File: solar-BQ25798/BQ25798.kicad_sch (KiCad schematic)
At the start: 34 parts, among them U1701 BQ25798RQMR

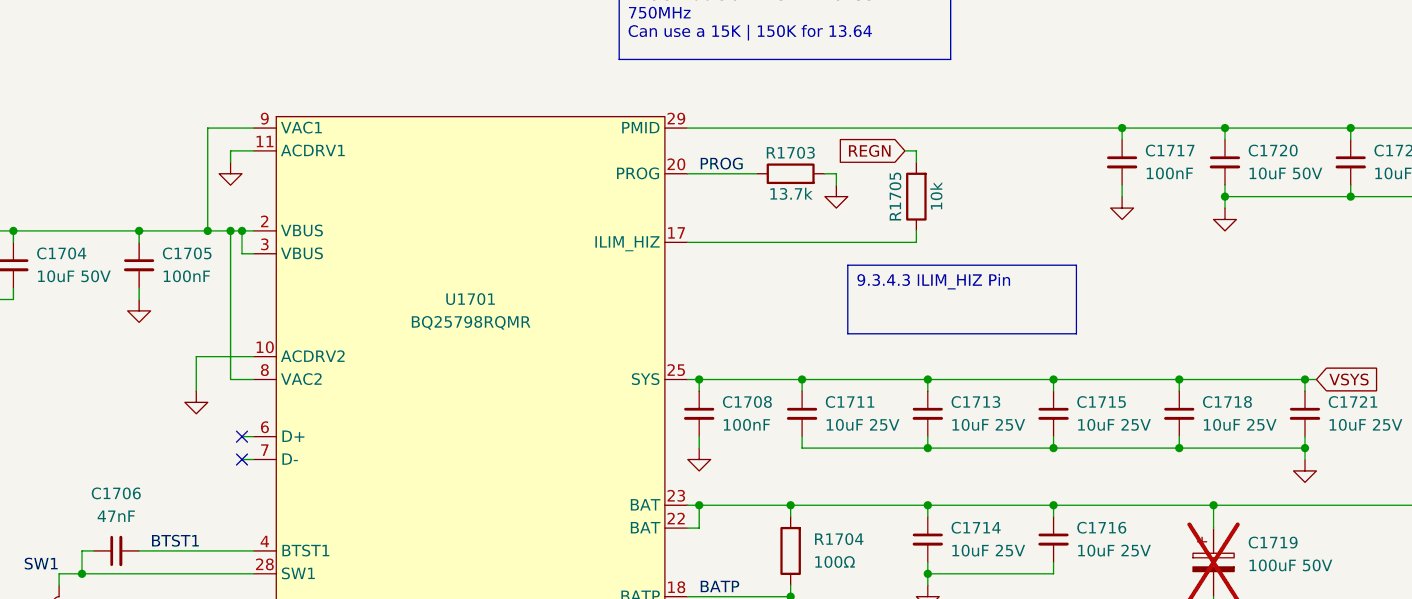
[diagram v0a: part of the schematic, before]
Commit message: Reduce number of different resistor and capacitor values
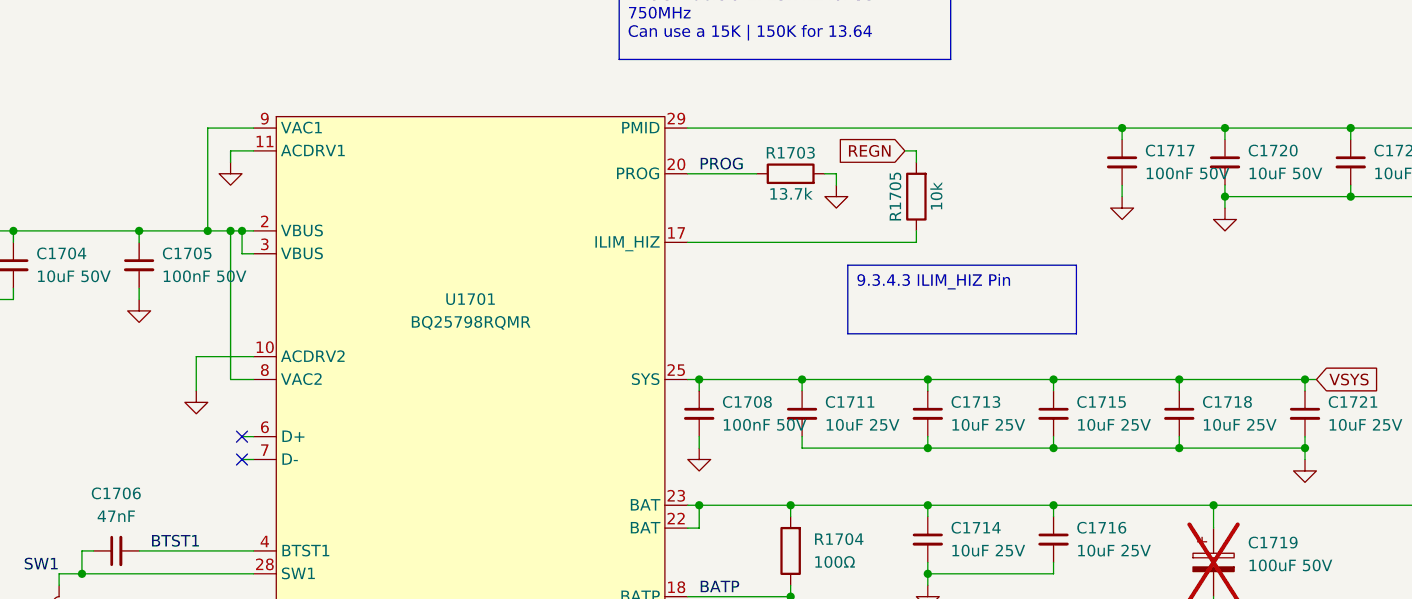
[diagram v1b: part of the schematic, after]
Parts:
- C1705, C1708, C1717: value 100nF -> 100nF 50V
- C1709: footprint Capacitor_SMD:C_0603_1608Metric -> Capacitor_SMD:C_0402_1005Metric; LCSC Part C19666 -> C23733
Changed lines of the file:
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@@
 			)
 		)
-		(property "Value" "100nF"
+		(property "Value" "100nF 50V"
 			(at 233.68 43.1862 0)
 			(show_name no)
@@
 			)
 		)
-		(property "Value" "100nF"
+		(property "Value" "100nF 50V"
 			(at 124.46 54.6162 0)
 			(show_name no)
@@
 			)
 		)
-		(property "Value" "100nF"
+		(property "Value" "100nF 50V"
 			(at 186.69 71.1262 0)
 			(show_name no)
@@
 			)
 		)
-		(property "Footprint" "Capacitor_SMD:C_0603_1608Metric"
+		(property "Footprint" "Capacitor_SMD:C_0402_1005Metric"
 			(at 187.96 127 0)
 			(hide yes)
@@
 			)
 		)
-		(property "LCSC Part" "C19666"
+		(property "LCSC Part" "C23733"
 			(at 187.96 127 0)
 			(hide yes)

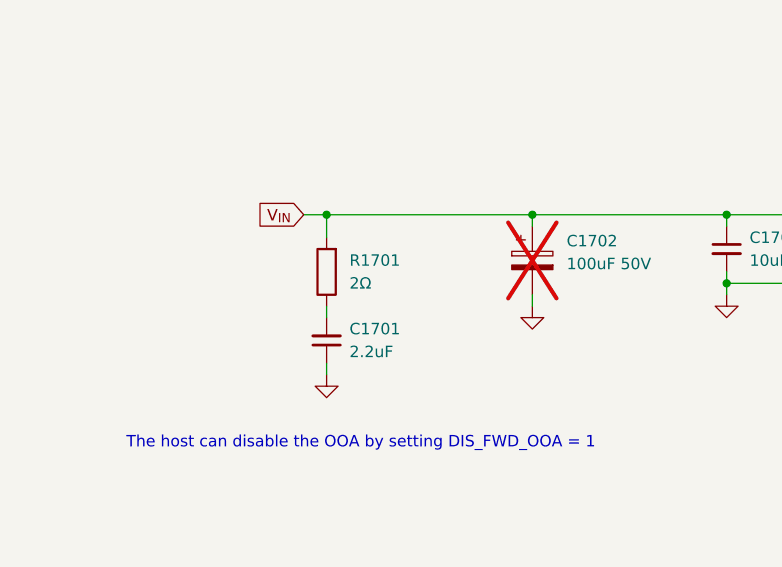
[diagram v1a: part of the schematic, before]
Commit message: Update components LCSC parts
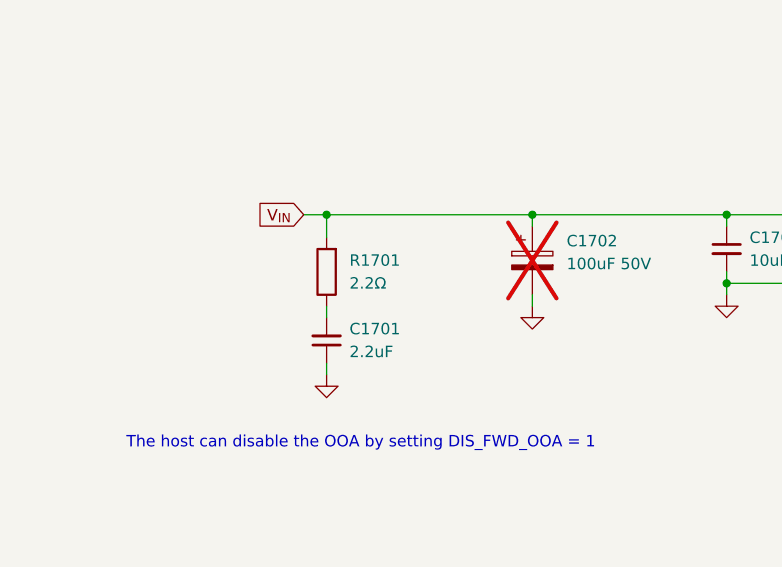
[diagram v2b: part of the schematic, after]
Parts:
- R1701: value 2Ω -> 2.2Ω; LCSC Part C17606 -> C17521
- R1707: LCSC Part C477765 -> C5948099
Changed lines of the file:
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@@
 			)
 		)
-		(property "Value" "2Ω"
+		(property "Value" "2.2Ω"
 			(at 52.07 57.1499 0)
 			(show_name no)
@@
 			)
 		)
-		(property "LCSC Part" "C17606"
+		(property "LCSC Part" "C17521"
 			(at 49.53 55.88 0)
 			(hide yes)
@@
 			)
 		)
-		(property "LCSC Part" "C477765"
+		(property "LCSC Part" "C5948099"
 			(at 217.17 109.22 0)
 			(hide yes)

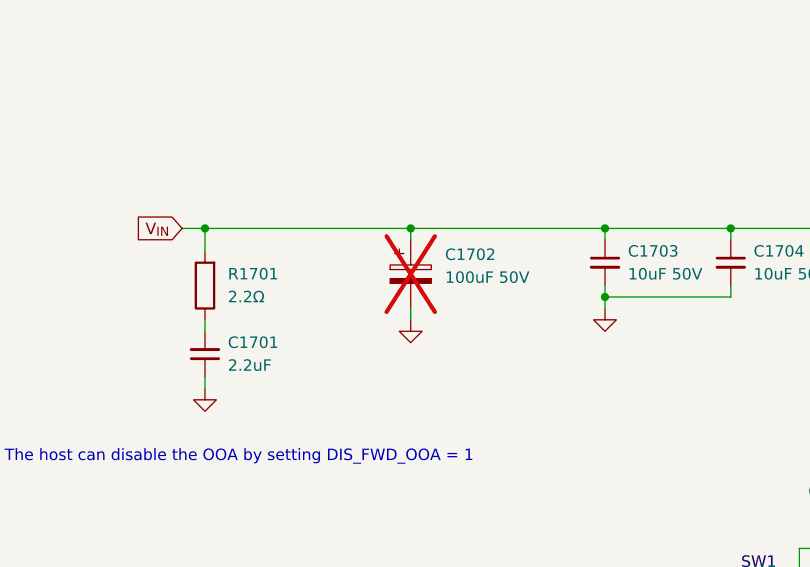
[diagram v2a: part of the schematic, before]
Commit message: Add heating element
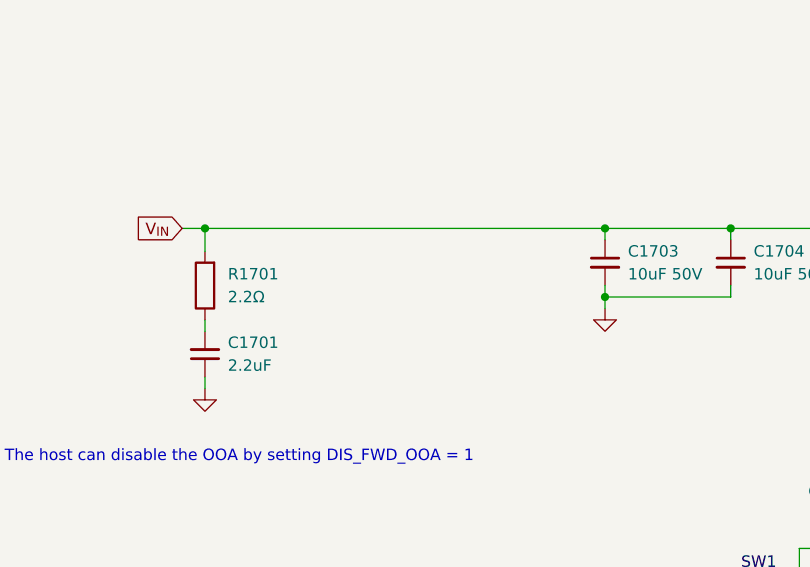
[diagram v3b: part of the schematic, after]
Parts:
- removed C1702: 100uF 50V, Capacitor_THT:CP_Radial_D6.3mm_P2.50mm, symbol Device:C_Polarized
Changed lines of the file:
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@@
 	)
 	(junction
-		(at 72.39 49.53)
-		(diameter 0)
-		(color 0 0 0 0)
-	)
-	(junction
 		(at 209.55 87.63)
 		(diameter 0)
@@
 	(wire
 		(pts
-			(xy 49.53 49.53) (xy 72.39 49.53)
-		)
-		(stroke
-			(width 0)
-			(type default)
-		)
-	)
-	(wire
-		(pts
-			(xy 72.39 49.53) (xy 72.39 50.8)
+			(xy 49.53 49.53) (xy 93.98 49.53)
 		)
 		(stroke
@@
 	(wire
 		(pts
-			(xy 72.39 49.53) (xy 93.98 49.53)
-		)
-		(stroke
-			(width 0)
-			(type default)
-		)
-	)
-	(wire
-		(pts
 			(xy 133.35 74.93) (xy 134.62 74.93)
 		)
@@
 	(wire
 		(pts
-			(xy 72.39 58.42) (xy 72.39 59.69)
-		)
-		(stroke
-			(width 0)
-			(type default)
-		)
-	)
-	(wire
-		(pts
 			(xy 132.08 66.04) (xy 134.62 66.04)
 		)
@@
 	)
 	(symbol
-		(lib_id "Device:C_Polarized")
-		(at 72.39 54.61 0)
-		(unit 1)
-		(body_style 1)
-		(exclude_from_sim no)
-		(in_bom no)
-		(on_board yes)
-		(in_pos_files yes)
-		(dnp yes)
-		(fields_autoplaced yes)
-		(property "Reference" "C1702"
-			(at 76.2 52.4509 0)
-			(show_name no)
-			(do_not_autoplace no)
-			(effects
-				(font
-					(size 1.27 1.27)
-				)
-				(justify left)
-			)
-		)
-		(property "Value" "100uF 50V"
-			(at 76.2 54.9909 0)
-			(show_name no)
-			(do_not_autoplace no)
-			(effects
-				(font
-					(size 1.27 1.27)
-				)
-				(justify left)
-			)
-		)
-		(property "Footprint" "Capacitor_THT:CP_Radial_D6.3mm_P2.50mm"
-			(at 73.3552 58.42 0)
-			(hide yes)
-			(show_name no)
-			(do_not_autoplace no)
-			(effects
-				(font
-					(size 1.27 1.27)
-				)
-			)
-		)
-		(property "Datasheet" ""
-			(at 72.39 54.61 0)
-			(hide yes)
-			(show_name no)
-			(do_not_autoplace no)
-			(effects
-				(font
-					(size 1.27 1.27)
-				)
-			)
-		)
-		(property "Description" "Polarized capacitor"
-			(at 72.39 54.61 0)
-			(hide yes)
-			(show_name no)
-			(do_not_autoplace no)
-			(effects
-				(font
-					(size 1.27 1.27)
-				)
-			)
-		)
-		(pin "2"
-		)
-		(pin "1"
-		)
-		(instances
-			(project "solar-BQ25798"
-				(path "/822b745e-d66e-4222-a6d2-360780548724/d84bfbfe-22f6-48d9-a29f-b45e9820ae80"
-					(reference "C1702")
-					(unit 1)
-				)
-			)
-		)
-	)
-	(symbol
 		(lib_id "Device:C_Small")
 		(at 198.12 105.41 270)
@@
 					(unit 1)
 				)
-			)
-		)
-	)
-	(symbol
-		(lib_id "power:GND")
-		(at 72.39 59.69 0)
-		(unit 1)
-		(body_style 1)
-		(exclude_from_sim no)
-		(in_bom yes)
-		(on_board yes)
-		(in_pos_files yes)
-		(dnp no)
-		(fields_autoplaced yes)
-		(property "Reference" "#PWR01702"
-			(at 72.39 66.04 0)
-			(hide yes)
-			(show_name no)
-			(do_not_autoplace no)
-			(effects
-				(font
-					(size 1.27 1.27)
-				)
-			)
-		)
-		(property "Value" "GND"
-			(at 72.39 64.77 0)
-			(hide yes)
-			(show_name no)
-			(do_not_autoplace no)
-			(effects
-				(font
-					(size 1.27 1.27)
-				)
-			)
-		)
-		(property "Footprint" ""
-			(at 72.39 59.69 0)
-			(hide yes)
-			(show_name no)
-			(do_not_autoplace no)
-			(effects
-				(font
-					(size 1.27 1.27)
-				)
-			)
-		)
-		(property "Datasheet" ""
-			(at 72.39 59.69 0)
-			(hide yes)
-			(show_name no)
-			(do_not_autoplace no)
-			(effects
-				(font
-					(size 1.27 1.27)
-				)
-			)
-		)
-		(property "Description" "Power symbol creates a global label with name \"GND\" , ground"
-			(at 72.39 59.69 0)
-			(hide yes)
-			(show_name no)
-			(do_not_autoplace no)
-			(effects
-				(font
-					(size 1.27 1.27)
-				)
-			)
-		)
-		(pin "1"
-		)
-		(instances
-			(project "solar-BQ25798"
-				(path "/822b745e-d66e-4222-a6d2-360780548724/d84bfbfe-22f6-48d9-a29f-b45e9820ae80"
-					(reference "#PWR01702")
-					(unit 1)
-				)
